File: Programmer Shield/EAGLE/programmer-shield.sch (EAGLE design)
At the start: 6 parts

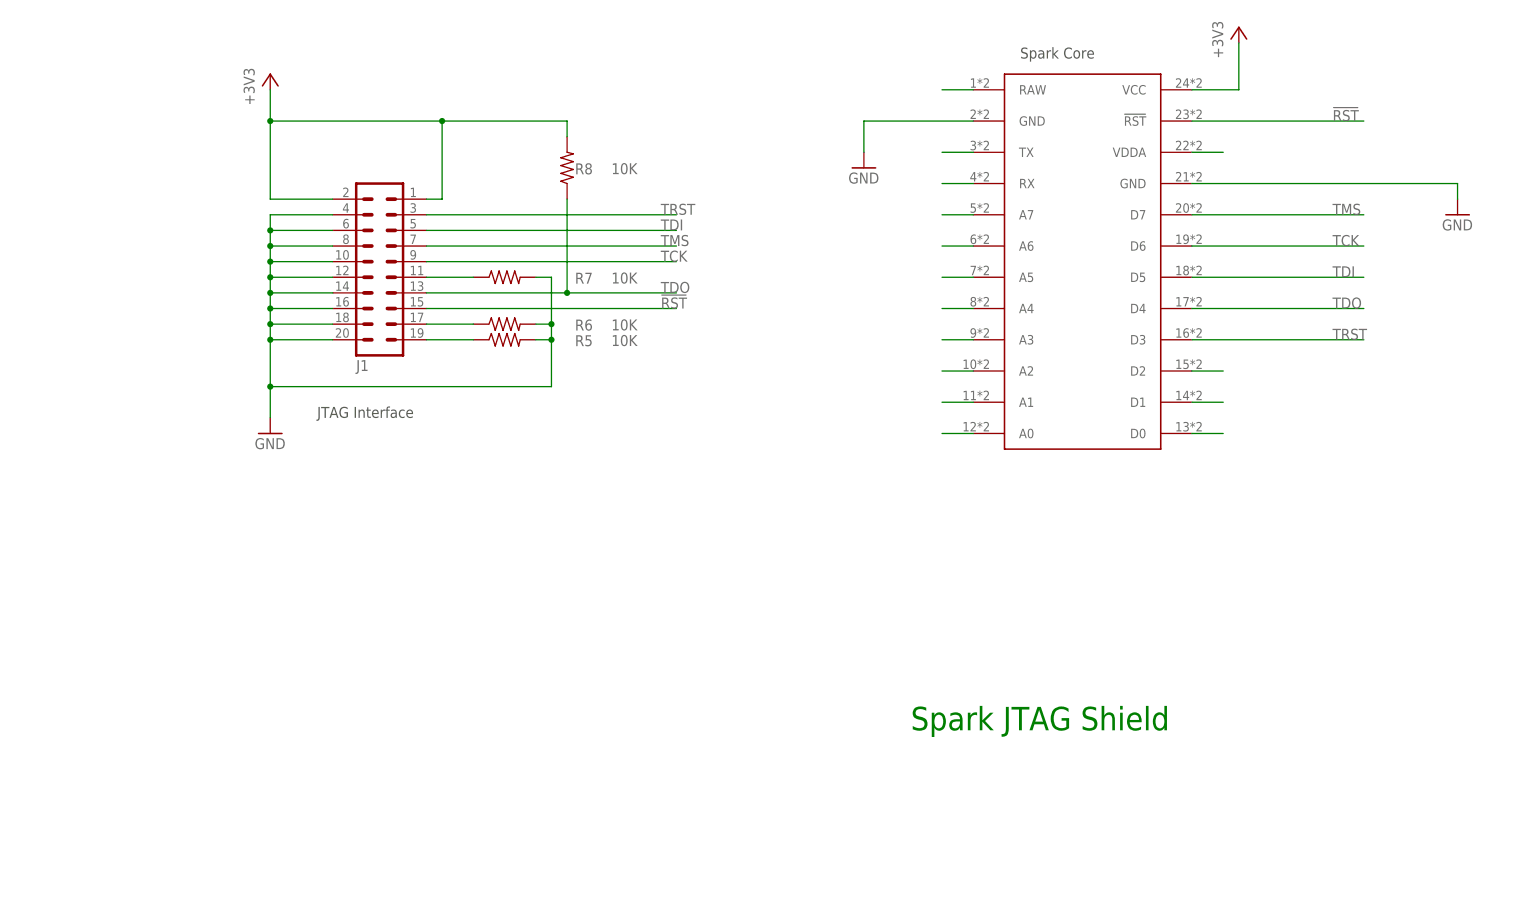
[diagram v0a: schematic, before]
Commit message: updated shield BOMs and boards
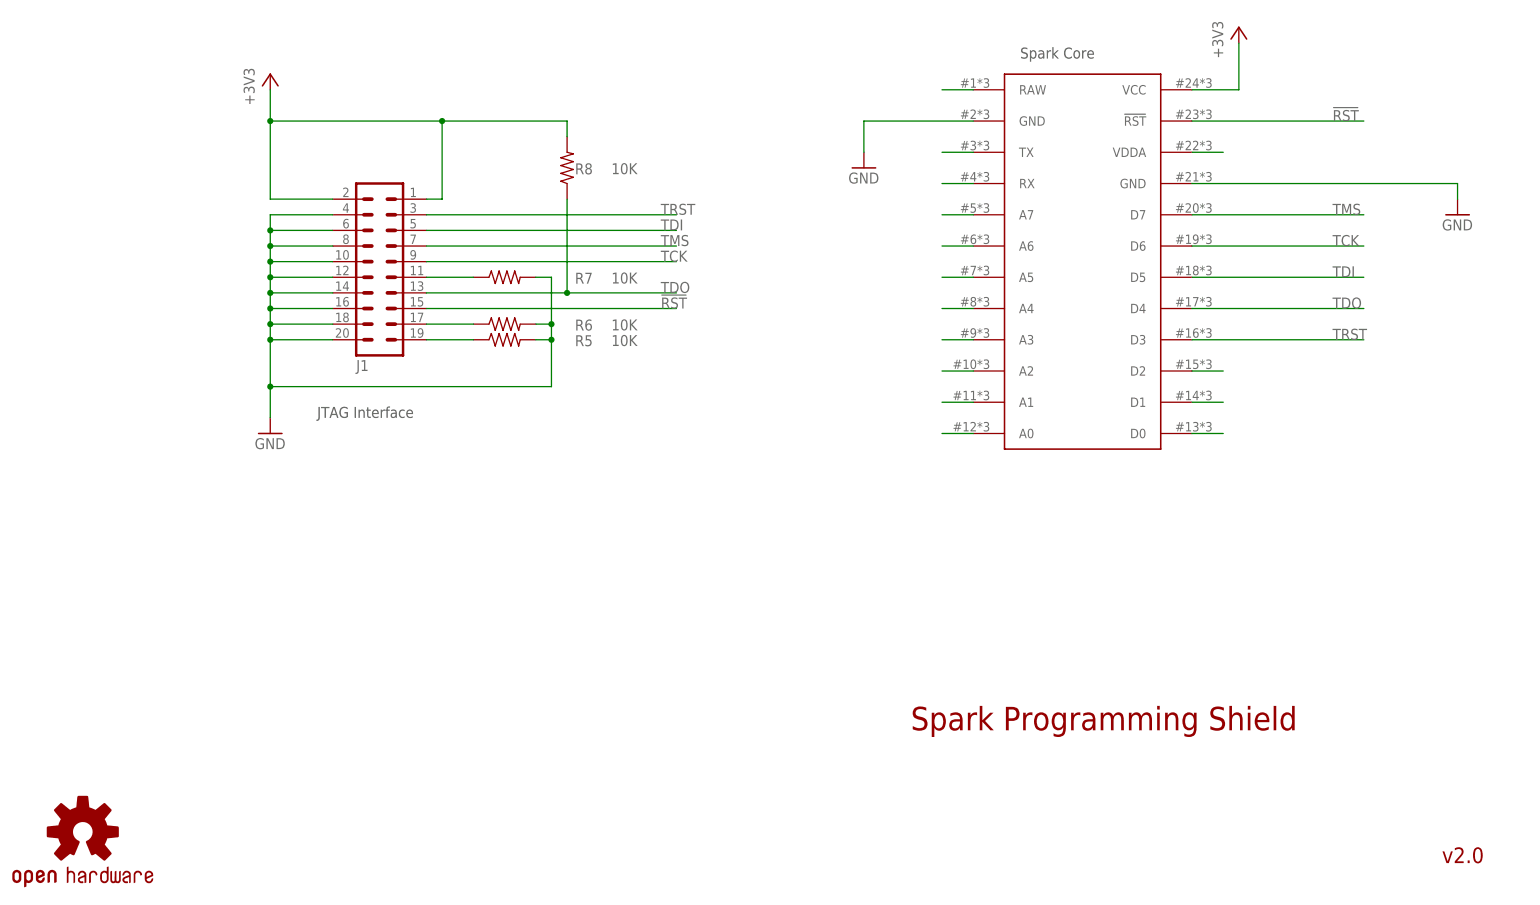
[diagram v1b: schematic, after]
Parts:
- added LOGO1: OSHW-LOGOM, Spark:OSHW-LOGOM
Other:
- note added: "Spark Programming Shield"
- note added: "v2.0"
- note removed: "Spark JTAG Shield"
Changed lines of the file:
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@@
 <setting verticaltext="up"/>
 </settings>
-<grid distance="0.1" unitdist="inch" unit="inch" style="lines" multiple="1" display="yes" altdistance="0.01" altunitdist="inch" altunit="inch"/>
+<grid distance="0.05" unitdist="inch" unit="inch" style="lines" multiple="1" display="no" altdistance="0.01" altunitdist="inch" altunit="inch"/>
 <layers>
 <layer number="1" name="Top" color="4" fill="1" visible="no" active="no"/>
@@
 <layer number="19" name="Unrouted" color="6" fill="1" visible="no" active="no"/>
 <layer number="20" name="Dimension" color="15" fill="1" visible="no" active="no"/>
-<layer number="21" name="tPlace" color="7" fill="1" visible="no" active="no"/>
-<layer number="22" name="bPlace" color="7" fill="1" visible="no" active="no"/>
+<layer number="21" name="tPlace" color="16" fill="1" visible="no" active="no"/>
+<layer number="22" name="bPlace" color="14" fill="1" visible="no" active="no"/>
 <layer number="23" name="tOrigins" color="15" fill="1" visible="no" active="no"/>
 <layer number="24" name="bOrigins" color="15" fill="1" visible="no" active="no"/>
@@
 <layer number="49" name="Reference" color="7" fill="1" visible="no" active="no"/>
 <layer number="50" name="dxf" color="7" fill="1" visible="no" active="no"/>
-<layer number="51" name="tDocu" color="7" fill="1" visible="no" active="no"/>
+<layer number="51" name="tDocu" color="6" fill="1" visible="no" active="no"/>
 <layer number="52" name="bDocu" color="7" fill="1" visible="no" active="no"/>
 <layer number="53" name="tGND_GNDA" color="7" fill="9" visible="no" active="no"/>
@@
 <part name="U$1" library="Spark" deviceset="SPARK_CORE" device=""/>
 <part name="FRAME2" library="frames" deviceset="LETTER_L" device=""/>
+<part name="LOGO1" library="Spark" deviceset="OSHW-LOGO" device="M"/>
 </parts>
 <sheets>
@@
 <text x="53.34" y="78.74" size="1.778" layer="97">JTAG Interface</text>
 <text x="167.64" y="137.16" size="1.778" layer="97">Spark Core</text>
-<text x="149.86" y="27.94" size="3.81" layer="91">Spark JTAG Shield</text>
+<text x="149.86" y="27.94" size="3.81" layer="94">Spark Programming Shield</text>
+<text x="236.22" y="6.35" size="2.54" layer="94">v2.0</text>
 </plain>
 <instances>
@@
 <instance part="FRAME2" gate="G$1" x="0" y="0"/>
 <instance part="FRAME2" gate="G$2" x="147.32" y="0"/>
+<instance part="LOGO1" gate="G$1" x="15.24" y="11.43"/>
 </instances>
 <busses>

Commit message: added license info to all design files
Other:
- note added: "Reference Designs ARE PROVIDED "AS IS" AND "WITH ALL FAULTS. SPARK LABS, INC ("SPARK") DISCLAIMS ALL OTHER WARRANTIES, EXPRESS OR IMPLIED, REGARDING PRODUCTS OR THE REFERENCE DESIGNS, INCLUDING BUT NOT LIMITED TO, ANY IMPLIED WARRANTIES OF MERCHANTABILITY, FITNESS FOR A PARTICULAR PURPOSE, OR NON-INFRINGEMENT. Spark may make changes to specifications and product descriptions at any time, without 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"
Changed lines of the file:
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@@
 <setting verticaltext="up"/>
 </settings>
-<grid distance="0.05" unitdist="inch" unit="inch" style="lines" multiple="1" display="no" altdistance="0.01" altunitdist="inch" altunit="inch"/>
+<grid distance="0.1" unitdist="inch" unit="inch" style="lines" multiple="1" display="no" altdistance="0.01" altunitdist="inch" altunit="inch"/>
 <layers>
 <layer number="1" name="Top" color="4" fill="1" visible="no" active="no"/>
@@
 <text x="149.86" y="27.94" size="3.81" layer="94">Spark Programming Shield</text>
 <text x="236.22" y="6.35" size="2.54" layer="94">v2.0</text>
+<text x="5.08" y="2.54" size="1.778" layer="95">Reference Designs ARE PROVIDED "AS IS" AND "WITH ALL FAULTS. SPARK LABS, INC
+("SPARK") DISCLAIMS ALL OTHER WARRANTIES, EXPRESS OR IMPLIED, REGARDING
+PRODUCTS OR THE REFERENCE DESIGNS, INCLUDING BUT NOT LIMITED TO, ANY
+IMPLIED WARRANTIES OF MERCHANTABILITY, FITNESS FOR A PARTICULAR PURPOSE,
+OR NON-INFRINGEMENT.
+Spark may make changes to specifications and product descriptions at any
+time, without notice. The Customer must not rely on the absence or
+characteristics of any features or instructions marked "reserved" or
+"undefined." Spark reserves these for future definition and shall have
+no responsibility whatsoever for conflicts or incompatibilities arising
+from future changes to them. The product information on the Web Site or
+Materials is subject to change without notice. Do not finalize a design
+with this information.
+Spark is a registered trademark.</text>
 </plain>
 <instances>
@@
 <instance part="FRAME2" gate="G$1" x="0" y="0"/>
 <instance part="FRAME2" gate="G$2" x="147.32" y="0"/>
-<instance part="LOGO1" gate="G$1" x="15.24" y="11.43"/>
+<instance part="LOGO1" gate="G$1" x="129.54" y="11.43"/>
 </instances>
 <busses>
@@
 </schematic>
 </drawing>
+<compatibility>
+<note version="6.3" minversion="6.2.2" severity="warning">
+Since Version 6.2.2 text objects can contain more than one line,
+which will not be processed correctly with this version.
+</note>
+</compatibility>
 </eagle>

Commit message: updated sshield and pshield gerbers
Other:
- note added: "v2.0.1"
- note removed: "v2.0"
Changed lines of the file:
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@@
 <?xml version="1.0" encoding="utf-8"?>
 <!DOCTYPE eagle SYSTEM "eagle.dtd">
-<eagle version="6.3">
+<eagle version="6.5.0">
 <drawing>
 <settings>
@@
 <text x="167.64" y="137.16" size="1.778" layer="97">Spark Core</text>
 <text x="149.86" y="27.94" size="3.81" layer="94">Spark Programming Shield</text>
-<text x="236.22" y="6.35" size="2.54" layer="94">v2.0</text>
+<text x="236.22" y="6.35" size="2.54" layer="94">v2.0.1</text>
 <text x="5.08" y="2.54" size="1.778" layer="95">Reference Designs ARE PROVIDED "AS IS" AND "WITH ALL FAULTS. SPARK LABS, INC
 ("SPARK") DISCLAIMS ALL OTHER WARRANTIES, EXPRESS OR IMPLIED, REGARDING
